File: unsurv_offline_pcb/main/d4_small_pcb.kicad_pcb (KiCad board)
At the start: 4 copper layers, 32 x 45 mm, 52 parts, among them J1 U_FL-R-SMT-1_10_, J2 S2B-PH-SM4-TB_LF__SN_, Q1 UMH3N, U1 TTGO-Micro32-ESP32, U3 CAM-M8C-0-10, U4 AP2112K-3.3, U5 CH340G, U6 RF430CL330H, U7 BMA400-I2C, U8 RFM95W-868S2, U9 PQ2581DLHT

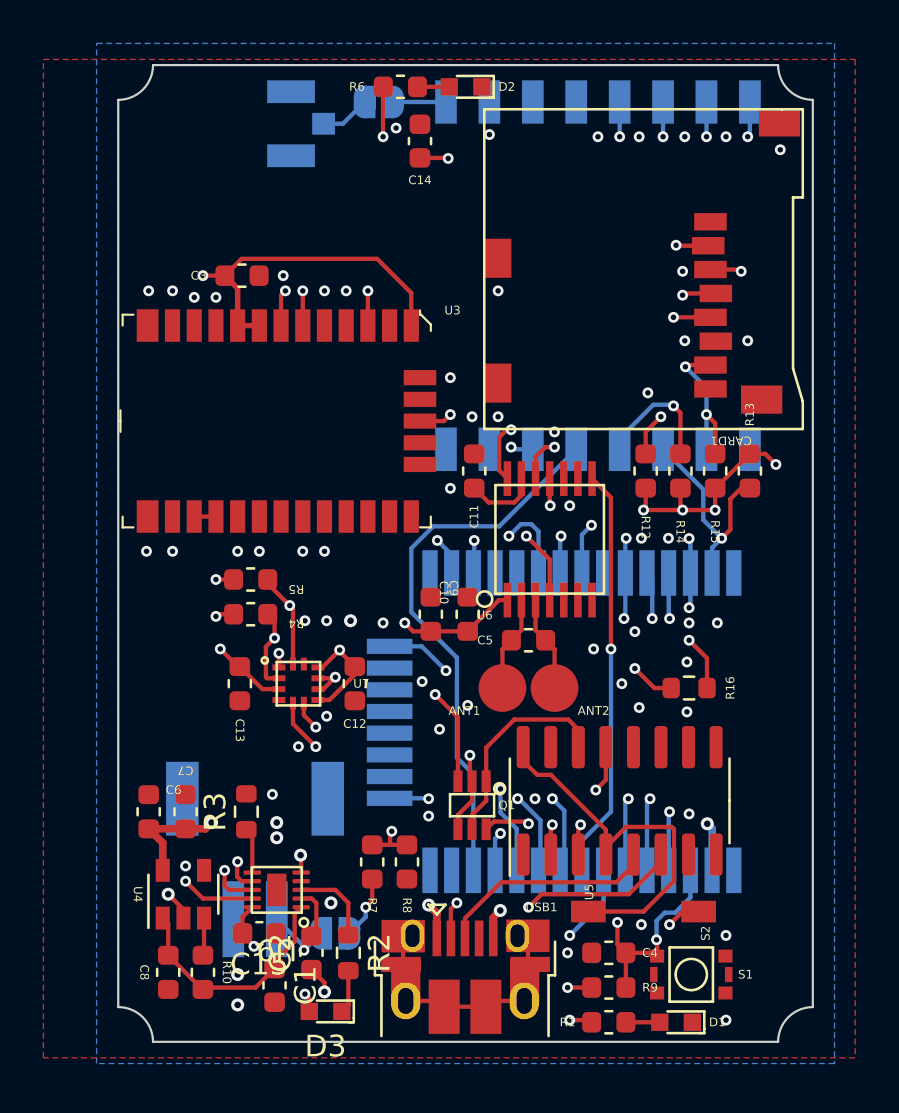
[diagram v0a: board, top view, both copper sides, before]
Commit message: moving passives around BQ25181
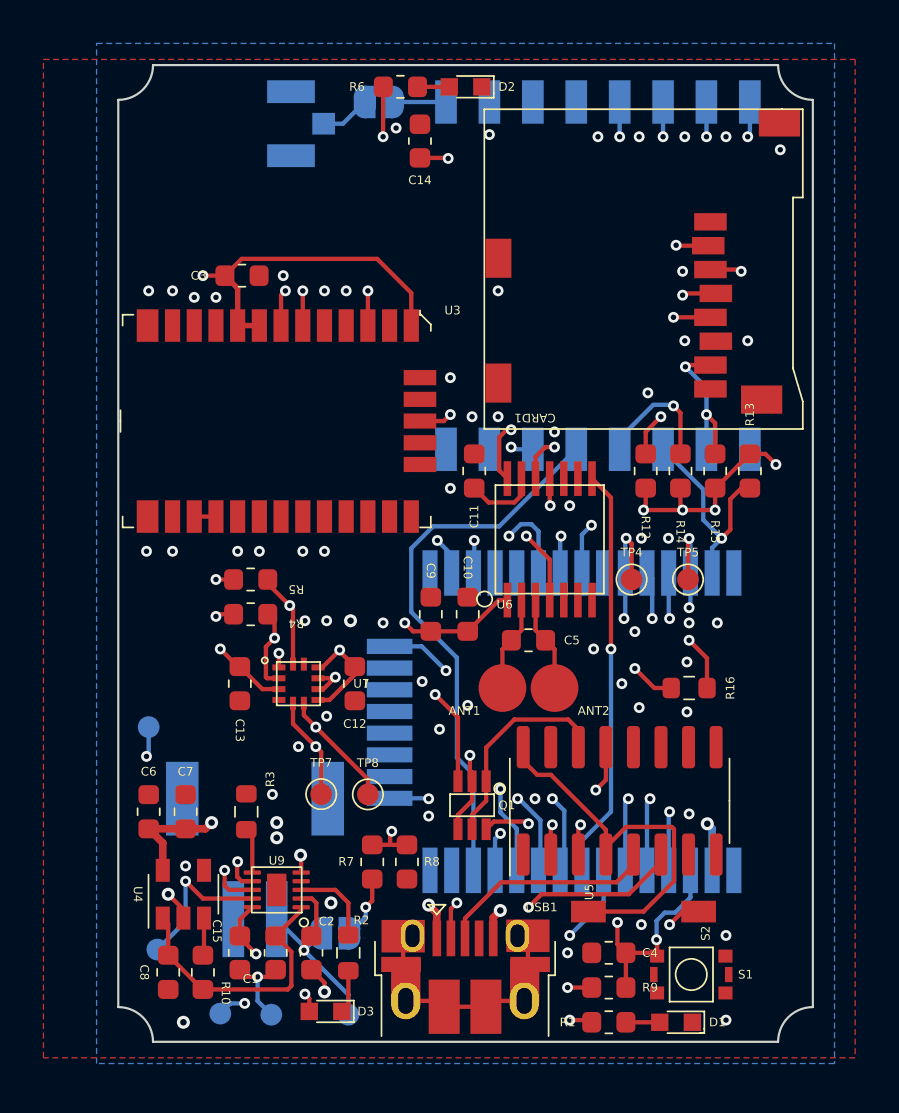
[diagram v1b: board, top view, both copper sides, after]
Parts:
- added TP1: GND, TestPoint:TestPoint_Pad_D1.0mm, B.Cu at (25.1, 63.8)
- added TP2: 5V, TestPoint:TestPoint_Pad_D1.0mm, B.Cu at (22.7, 63.7)
- added TP3: 3V3, TestPoint:TestPoint_Pad_D1.0mm, B.Cu at (19.4, 50.5)
- added TP4: SDA, TestPoint:TestPoint_Pad_D1.0mm, F.Cu at (41.6, 43.7)
- added TP5: SCL, TestPoint:TestPoint_Pad_D1.0mm, F.Cu at (44.2, 43.7)
- added TP6: BATT, TestPoint:TestPoint_Pad_D1.0mm, B.Cu at (28.6, 63.8)
- added TP7: ACC1, TestPoint:TestPoint_Pad_D1.0mm, F.Cu at (27.4, 53.6)
- added TP8: ACC2, TestPoint:TestPoint_Pad_D1.0mm, F.Cu at (29.5, 53.6)
- added TP9: TI_BATT_INT, TestPoint:TestPoint_Pad_D1.0mm, B.Cu at (19.8, 60.8)
- moved C1 1.50 mm to (25.2, 60.9)
- moved C15 1.27 mm to (23.6, 60.9), turned to 90 degrees
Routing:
- net ACC_INT2: track 15.1 -> 19.2 mm
- net GND: track 10.1 -> 14.1 mm
- net +BATT: track 6.27 -> 10.1 mm
- net 36: track 29.8 -> 33.5 mm
- net ACC_INT1: track 16.6 -> 18.9 mm
- net SDA: track 71.2 -> 73.2 mm
- net SCL: track 82.3 -> 84.2 mm
- net +5V: track 4.78 -> 6.67 mm, vias 3 -> 4
- net VCC: track 11.1 -> 12.8 mm
- net +3V3: track 66.2 -> 67.6 mm, vias 21 -> 22
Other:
- board text added: "unsurv offline v0.4 pre production"
- board text removed: "unsurv offline v0.3.1 pre production"

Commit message: update RF430 package to VQFN
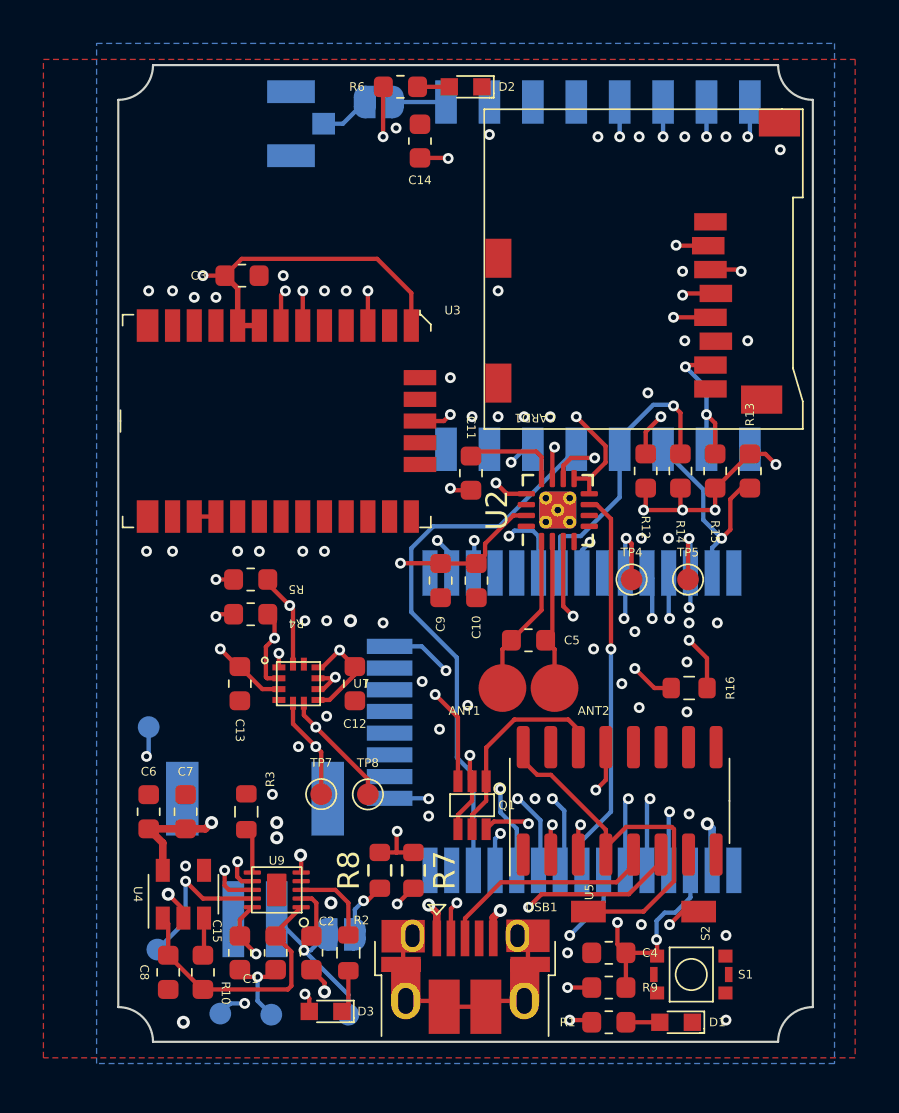
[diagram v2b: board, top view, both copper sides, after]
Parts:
- removed U6: RF430CL330H, unsurv_offline_pcb_footprints:RF430CL330H
- added U2: RF430CL330HIRGTR‎, unsurv_offline_pcb_footprints:RF430_3x3mm, F.Cu at (38.2, 40.5)
- moved R7 1.94 mm to (31.6, 57.1), turned to -90 degrees
- moved C9 1.61 mm to (32.9, 43.8), turned to -90 degrees
- moved C10 1.60 mm to (34.5, 43.8), turned to -90 degrees
- moved R8 1.31 mm to (30.1, 57.1), turned to 90 degrees
- moved JP1 0.25 mm to (28.2, 60.0)
- moved C11 0.18 mm to (34.2, 38.8), turned to -90 degrees
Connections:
- R7 pad 1: Net-(JP1-Pad2) -> 35
- R7 pad 2: 35 -> GND
- R8 pad 1: 35 -> Net-(JP1-Pad2)
- R8 pad 2: GND -> 35
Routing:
- net GND: track 14.1 -> 20.1 mm, vias 67 -> 69
- net ANT1: track 4.41 -> 7.50 mm
- net ANT2: track 4.41 -> 7.05 mm
- net SDA: track 73.2 -> 70.6 mm
- net 18: track 21.6 -> 20.0 mm, vias 3 -> 2
- net +3V3: track 67.6 -> 69.2 mm
- net 13: track 39.7 -> 41.2 mm
- net SCL: track 84.2 -> 85.7 mm
- net Net-(C11-Pad1): track 3.36 -> 4.44 mm
- net 32: track 19.0 -> 18.0 mm
- net 15: track 14.4 -> 13.6 mm

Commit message: reorganize passives
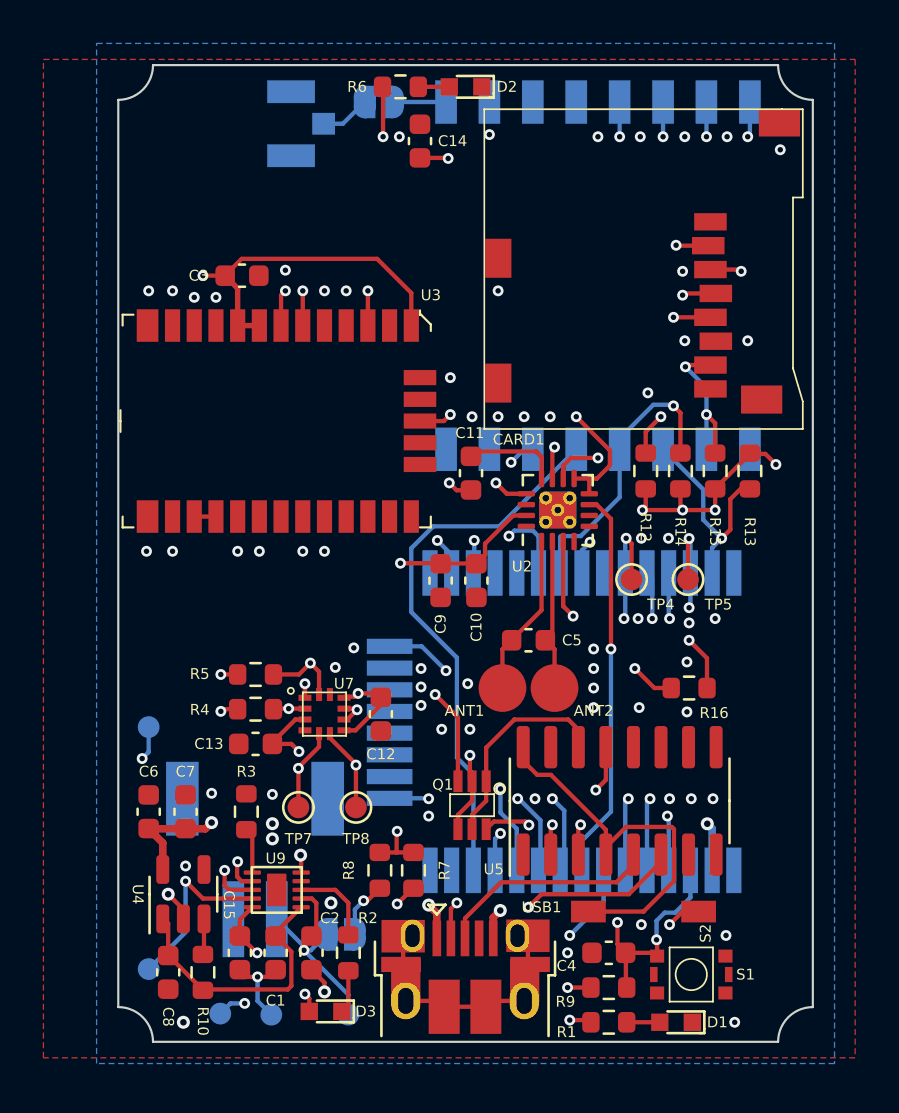
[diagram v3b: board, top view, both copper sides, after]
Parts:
- U3: footprint unsurv_offline_pcb_footprints:GPS_Module_CAM-M8C-0 -> digikey-footprints:GPS_Module_CAM-M8C-0
- U9: footprint unsurv_offline_pcb_footprints:BQ2581DLHT -> unsurv:BQ2581DLHT
- moved R4 4.38 mm to (24.3, 49.7)
- moved R5 4.38 mm to (24.3, 48.1)
- moved C13 2.87 mm to (24.3, 51.3), turned to 180 degrees
- moved C12 1.84 mm to (30.1, 49.9)
- moved U7 1.84 mm to (27.5, 49.9)
- moved TP7 1.21 mm to (26.3, 54.2)
- moved TP9 0.98 mm to (19.4, 61.6)
- moved TP8 0.81 mm to (28.9, 54.2)
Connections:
- C14 pad 2: +3V3 -> +3.3V
- U8 pad 13: +3V3 -> +3.3V
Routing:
- net +3V3: track 69.2 -> 57.4 mm, vias 22 -> 19
- net +3.3V: track 0.00 -> 11.2 mm, vias 0 -> 2
- net ACC_INT2: track 19.2 -> 15.1 mm
- net SDA: track 70.6 -> 66.8 mm
- net SCL: track 85.7 -> 82.7 mm
- net 36: track 33.5 -> 34.3 mm
- net 18: track 20.0 -> 19.1 mm
- net ACC_INT1: track 18.9 -> 18.4 mm
- net GND: track 20.1 -> 20.2 mm, vias 69 -> 74

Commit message: Update d4_small_pcb.kicad_pcb
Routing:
- net GND: vias 74 -> 73
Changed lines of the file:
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@@
   (via (at 20.5 30.4) (size 0.5) (drill 0.25) (layers "F.Cu" "B.Cu") (net 4))
   (via (at 42.1 59.6) (size 0.5) (drill 0.25) (layers "F.Cu" "B.Cu") (net 4))
-  (via (at 39.9 48.7) (size 0.5) (drill 0.25) (layers "F.Cu" "B.Cu") (net 4))
   (via (at 34.2 50.6) (size 0.5) (drill 0.25) (layers "F.Cu" "B.Cu") (net 4))
   (via (at 27.5 62.7) (size 0.6) (drill 0.3) (layers "F.Cu" "B.Cu") (net 4))
@@
   (via (at 35.1 23.2) (size 0.5) (drill 0.25) (layers "F.Cu" "B.Cu") (net 4))
   (via (at 29 49.7) (size 0.5) (drill 0.25) (layers "F.Cu" "B.Cu") (net 4))
-  (via (at 39.9 49.6) (size 0.5) (drill 0.25) (layers "F.Cu" "B.Cu") (net 4))
   (via (at 21.5 30.7) (size 0.5) (drill 0.25) (layers "F.Cu" "B.Cu") (net 4))
   (via (at 42.1 41.8) (size 0.5) (drill 0.25) (layers "F.Cu" "B.Cu") (net 4))
@@
   (via (at 25.1 53.6) (size 0.5) (drill 0.25) (layers "F.Cu" "B.Cu") (net 4))
   (via (at 28 47.75) (size 0.5) (drill 0.25) (layers "F.Cu" "B.Cu") (net 4))
-  (via (at 39.9 47.8) (size 0.5) (drill 0.25) (layers "F.Cu" "B.Cu") (net 4))
+  (via (at 41.55 46.9) (size 0.5) (drill 0.25) (layers "F.Cu" "B.Cu") (net 4))
   (via (at 42 49.6) (size 0.5) (drill 0.25) (layers "F.Cu" "B.Cu") (net 4))
   (via (at 24.417052 62.009055) (size 0.5) (drill 0.25) (layers "F.Cu" "B.Cu") (net 4))
@@
   (via (at 31.95 48.65) (size 0.5) (drill 0.25) (layers "F.Cu" "B.Cu") (net 4))
   (via (at 34.3 36.2) (size 0.5) (drill 0.25) (layers "F.Cu" "B.Cu") (net 4))
+  (via (at 41.2 48) (size 0.5) (drill 0.25) (layers "F.Cu" "B.Cu") (net 4))
   (via (at 26.5 42.4) (size 0.5) (drill 0.25) (layers "F.Cu" "B.Cu") (net 4))
   (via (at 33.25 39.25) (size 0.5) (drill 0.25) (layers "F.Cu" "B.Cu") (net 4))
@@
   (segment (start 45.5 39.4875) (end 45.5 40.5) (width 0.2) (layer "F.Cu") (net 7))
   (segment (start 23.5375 49.675) (end 22.825 49.675) (width 0.2) (layer "F.Cu") (net 7))
+  (segment (start 42.025 48.025) (end 42.7 48.7) (width 0.2) (layer "F.Cu") (net 7))
   (segment (start 43.9 40.4) (end 44 40.5) (width 0.2) (layer "F.Cu") (net 7))
   (segment (start 31.5 30.5) (end 29.92548 28.92548) (width 0.2) (layer "F.Cu") (net 7))
   (segment (start 38.7 62.5) (end 39.8125 62.5) (width 0.2) (layer "F.Cu") (net 7))
-  (segment (start 42.7 48.7) (end 41.8 47.8) (width 0.2) (layer "F.Cu") (net 7))
   (segment (start 23.5 32) (end 24.5 32) (width 0.25) (layer "F.Cu") (net 7))
   (segment (start 25.1 51.21) (end 25.1 51.275) (width 0.2) (layer "F.Cu") (net 7))
@@
   (segment (start 28.9 49.1) (end 28.45 49.1) (width 0.2) (layer "F.Cu") (net 7))
   (segment (start 20.05 55.8375) (end 20.05 57.1) (width 0.35) (layer "F.Cu") (net 7))
+  (segment (start 42.7 48.7) (end 43.475 48.7) (width 0.2) (layer "F.Cu") (net 7))
   (segment (start 22.0125 55.1875) (end 19.4 55.1875) (width 0.35) (layer "F.Cu") (net 7))
   (segment (start 30.1 49.1125) (end 30.1 49.479556) (width 0.2) (layer "F.Cu") (net 7))
@@
   (segment (start 47.8125 37.9125) (end 48.3 38.4) (width 0.2) (layer "F.Cu") (net 7))
   (segment (start 28.929556 50.65) (end 28.4 50.65) (width 0.2) (layer "F.Cu") (net 7))
-  (segment (start 43.475 48.7) (end 42.7 48.7) (width 0.2) (layer "F.Cu") (net 7))
   (segment (start 45.5 39.4875) (end 45.525 39.4875) (width 0.2) (layer "F.Cu") (net 7))
   (segment (start 42.3 40.35) (end 42.3 39.4875) (width 0.2) (layer "F.Cu") (net 7))
@@
   (via (at 22.725 48.075) (size 0.5) (drill 0.25) (layers "F.Cu" "B.Cu") (net 7))
   (via (at 38.7 62.5) (size 0.5) (drill 0.25) (layers "F.Cu" "B.Cu") (net 7))
-  (via (at 41.8 47.8) (size 0.5) (drill 0.25) (layers "F.Cu" "B.Cu") (net 7))
+  (via (at 42.025 48.025) (size 0.5) (drill 0.25) (layers "F.Cu" "B.Cu") (net 7))
   (via (at 43.4 59.6) (size 0.5) (drill 0.25) (layers "F.Cu" "B.Cu") (net 7))
   (via (at 45.5 40.5) (size 0.5) (drill 0.25) (layers "F.Cu" "B.Cu") (net 7))
@@
   (segment (start 34.95 51.45) (end 34.95 52.995) (width 0.2) (layer "F.Cu") (net 16))
   (segment (start 34.3 53.895978) (end 33.65 54.545978) (width 0.2) (layer "F.Cu") (net 17))
-  (segment (start 40.465 51.425) (end 40.465 52.935) (width 0.2) (layer "F.Cu") (net 17))
   (segment (start 33.65 54.545978) (end 33.65 55.205) (width 0.2) (layer "F.Cu") (net 17))
   (segment (start 34.3 52.995) (end 34.3 53.895978) (width 0.2) (layer "F.Cu") (net 17))
+  (segment (start 39.85 53.7) (end 40.465 53.085) (width 0.2) (layer "F.Cu") (net 17))
+  (segment (start 40.465 53.085) (end 40.465 51.425) (width 0.2) (layer "F.Cu") (net 17))
   (segment (start 34.2 51.8) (end 34.2 52.895) (width 0.2) (layer "F.Cu") (net 17))
   (segment (start 34.2 52.895) (end 34.3 52.995) (width 0.2) (layer "F.Cu") (net 17))
-  (segment (start 40.465 52.935) (end 40 53.4) (width 0.2) (layer "F.Cu") (net 17))
-  (via (at 40 53.4) (size 0.5) (drill 0.25) (layers "F.Cu" "B.Cu") (net 17))
+  (via (at 39.85 53.7) (size 0.5) (drill 0.25) (layers "F.Cu" "B.Cu") (net 17))
   (via (at 34.2 51.8) (size 0.5) (drill 0.25) (layers "F.Cu" "B.Cu") (net 17))
-  (segment (start 39.4 52.8) (end 40 53.4) (width 0.2) (layer "In1.Cu") (net 17))
+  (segment (start 39.85 53.7) (end 38.95 52.8) (width 0.2) (layer "In1.Cu") (net 17))
+  (segment (start 38.95 52.8) (end 35.2 52.8) (width 0.2) (layer "In1.Cu") (net 17))
   (segment (start 35.2 52.8) (end 34.2 51.8) (width 0.2) (layer "In1.Cu") (net 17))
-  (segment (start 35.2 52.8) (end 39.4 52.8) (width 0.2) (layer "In1.Cu") (net 17))
   (segment (start 32.6 49) (end 33.65 50.05) (width 0.2) (layer "F.Cu") (net 18))
   (segment (start 33.65 50.05) (end 33.65 52.995) (width 0.2) (layer "F.Cu") (net 18))

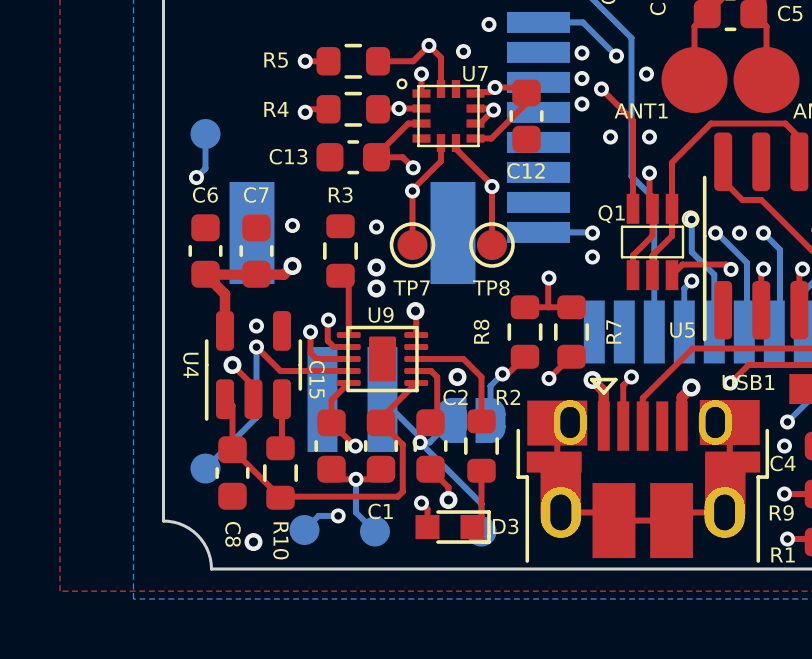
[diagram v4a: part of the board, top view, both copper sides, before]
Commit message: BQ25180 redesign
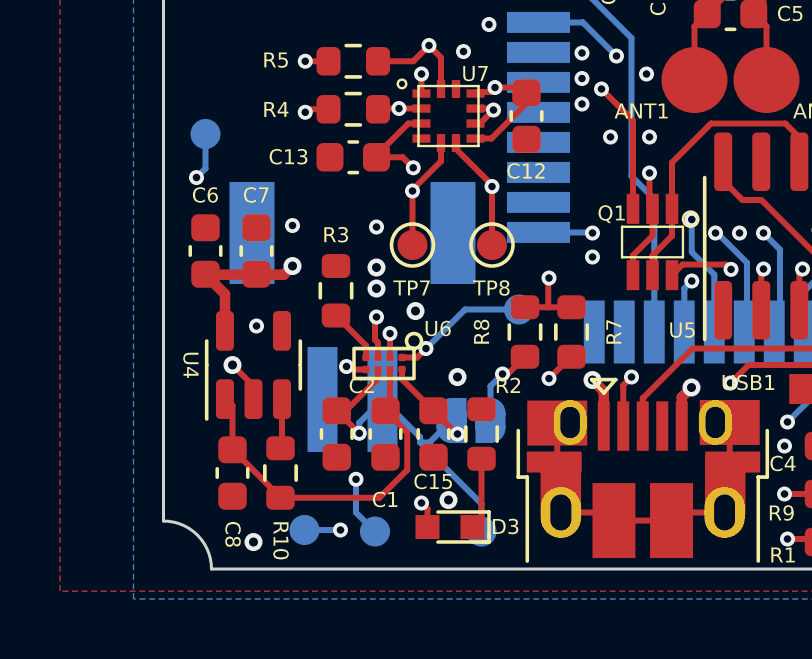
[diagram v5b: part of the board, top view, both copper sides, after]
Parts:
- removed U9: PQ2581DLHT, unsurv:BQ2581DLHT
- added U6: BQ25180, unsurv:BQ25180, F.Cu at (25.4, 58.1)
- moved TP9 11.7 mm to (29.9, 56.4)
- moved C15 3.42 mm to (27.0, 60.5)
- moved C2 3.15 mm to (23.8, 60.5)
- moved R3 1.33 mm to (23.8, 55.7)
- moved C1 0.43 mm to (25.4, 60.5)
- moved R2 0.40 mm to (28.6, 60.5)
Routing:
- net 36: track 34.3 -> 25.1 mm
- net Net-(R2-Pad1): track 3.90 -> 0.00 mm
- net GND: track 20.2 -> 16.9 mm, vias 73 -> 74
- net +BATT: track 10.3 -> 11.8 mm
